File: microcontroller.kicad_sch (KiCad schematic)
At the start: 29 parts, among them J2 Conn_ARM_JTAG_SWD_10, SW1 EN11-VSM, U8 STM32F051R4Tx, Y1 8MHz, Y2 32.768kHz

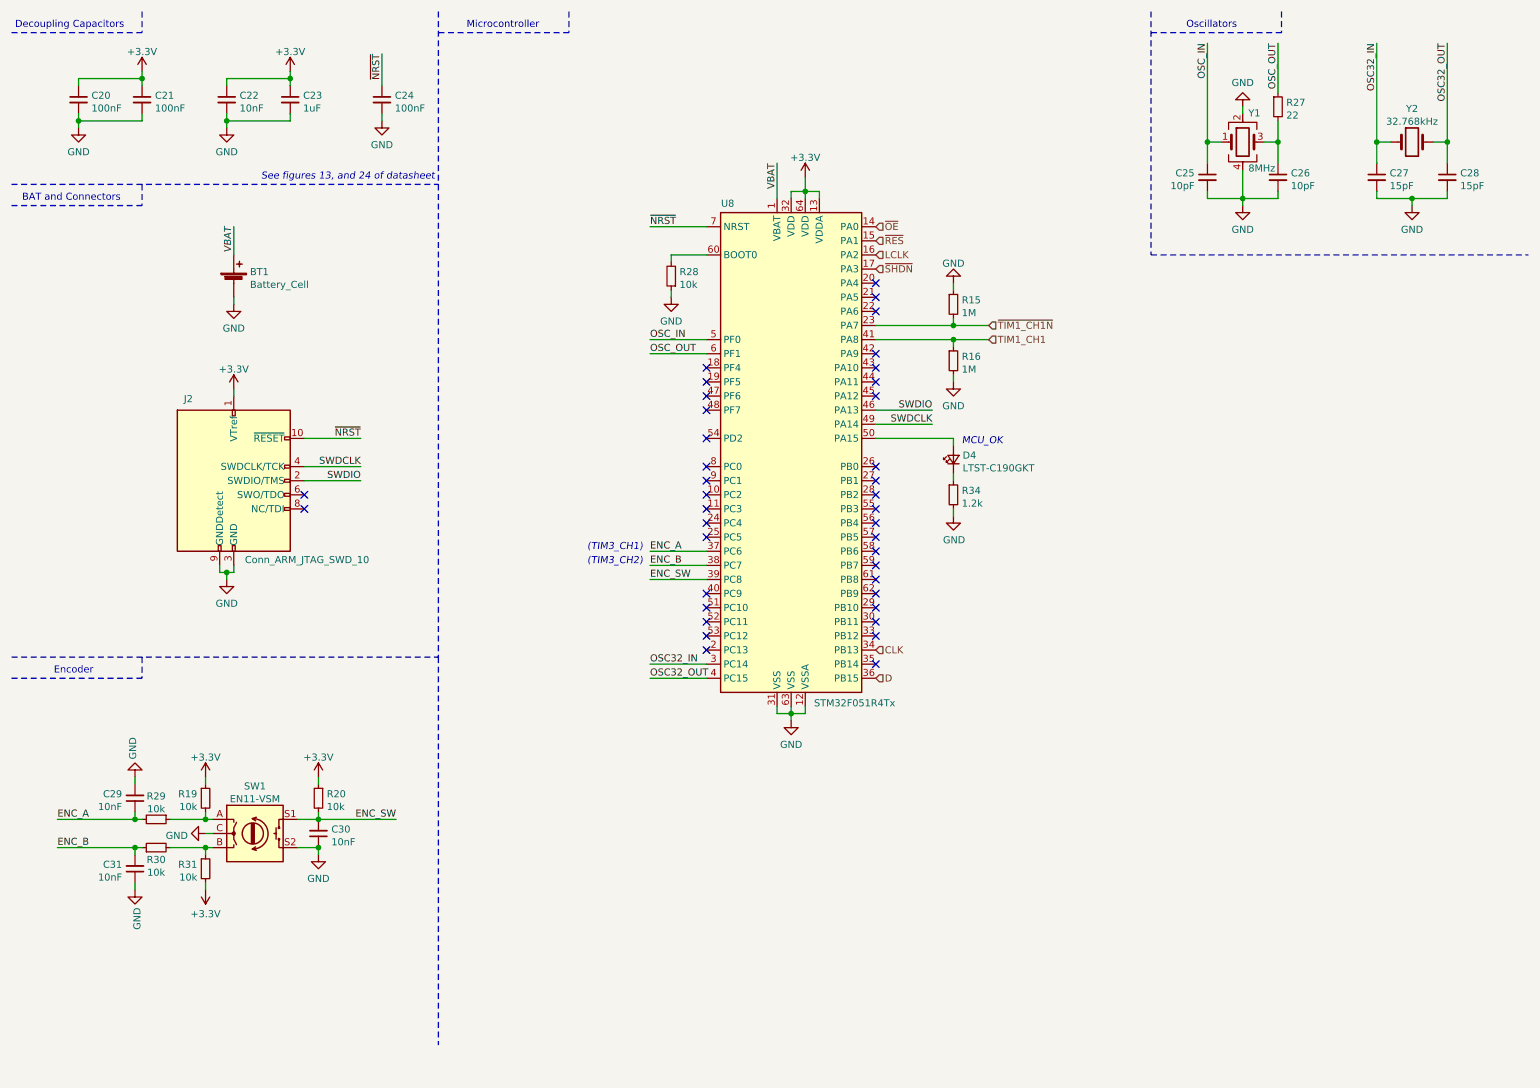
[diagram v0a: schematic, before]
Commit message: added outputs for schematic and gerber view
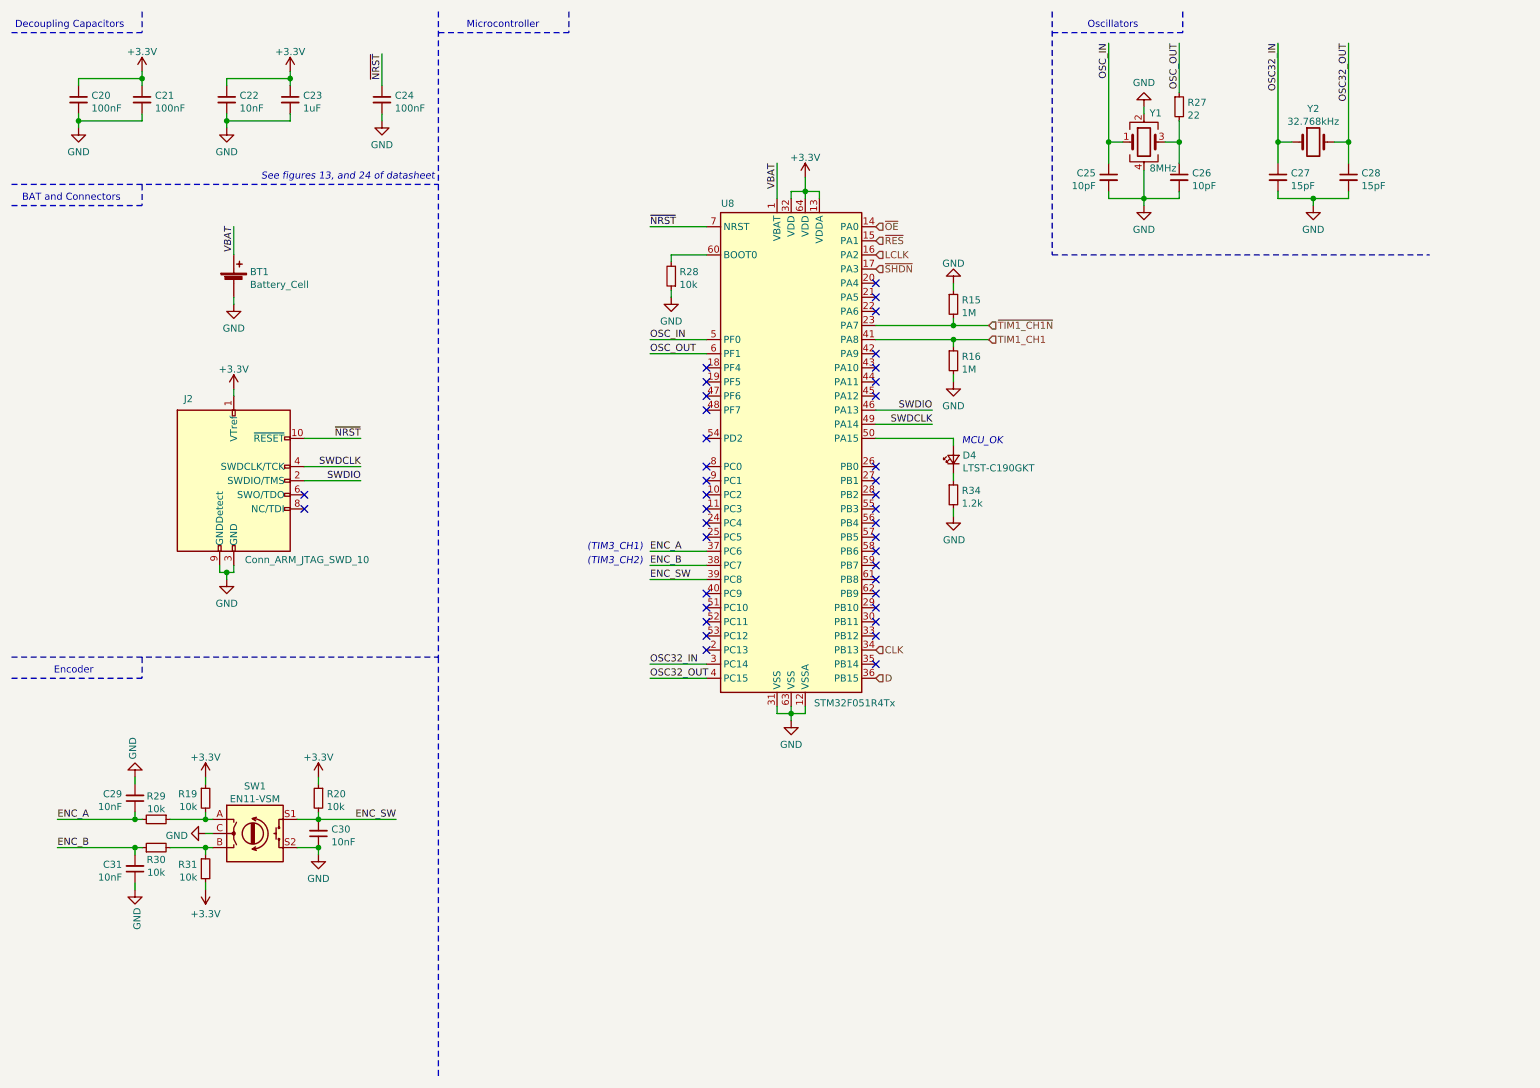
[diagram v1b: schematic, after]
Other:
- moved on the sheet: C25, C26, C27, C28, R27, Y1, Y2
